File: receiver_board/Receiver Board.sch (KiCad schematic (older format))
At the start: 12 parts, among them P4 SERIAL, SW1 SW_DPST, U1 LM3671, U2 ESP-01, U3 NeoPixel, U4 SN74LVC1T45

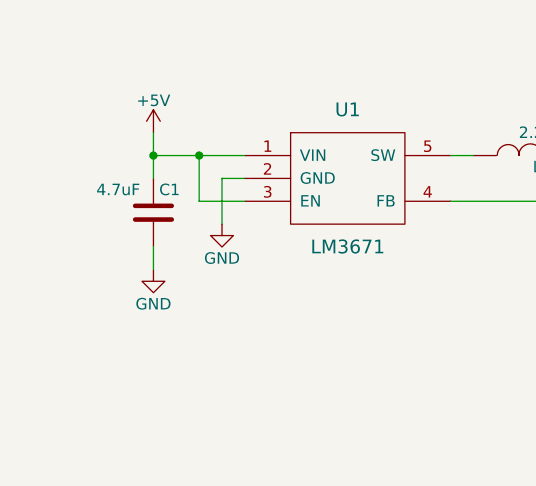
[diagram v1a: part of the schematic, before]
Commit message: Added BOM and fuse
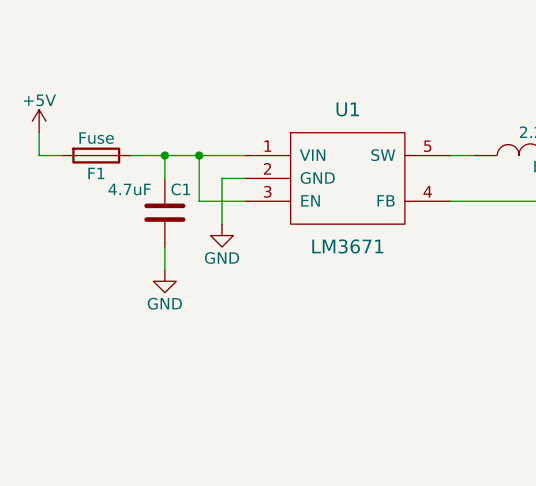
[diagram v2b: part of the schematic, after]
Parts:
- added F1: Fuse, Resistors_SMD:R_0805_HandSoldering, symbol Fuse
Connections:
- net +5V: now also F1.2; no longer C1.1, U1.1 (VIN), U1.3 (EN)
- new net: C1.1, F1.1, U1.1 (VIN), U1.3 (EN)
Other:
- moved on the sheet: C1
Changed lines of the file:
@@
 L C C1
 U 1 1 57A0E3BE
-P 3800 3250
-F 0 "C1" H 3825 3350 50  0000 L CNN
-F 1 "4.7uF" H 3550 3350 50  0000 L CNN
-F 2 "Capacitors_SMD:C_0805_HandSoldering" H 3800 4200 50  0001 C CNN
-F 3 "" H 3800 3250 50  0000 C CNN
-	1    3800 3250
+P 3850 3250
+F 0 "C1" H 3875 3350 50  0000 L CNN
+F 1 "4.7uF" H 3600 3350 50  0000 L CNN
+F 2 "Capacitors_SMD:C_0805_HandSoldering" H 3850 4200 50  0001 C CNN
+F 3 "" H 3850 3250 50  0000 C CNN
+	1    3850 3250
 	1    0    0    -1
 $EndComp
@@
 $EndComp
 $Comp
-L VCC #PWR6
+L VCC #PWR01
 U 1 1 5AF73AE7
 P 7350 2950
-F 0 "#PWR6" H 7350 2800 50  0001 C CNN
+F 0 "#PWR01" H 7350 2800 50  0001 C CNN
 F 1 "VCC" H 7350 3100 50  0000 C CNN
 F 2 "" H 7350 2950 50  0001 C CNN
@@
 $EndComp
 $Comp
-L GND #PWR8
+L GND #PWR02
 U 1 1 5AF73B1B
 P 8950 3950
-F 0 "#PWR8" H 8950 3700 50  0001 C CNN
+F 0 "#PWR02" H 8950 3700 50  0001 C CNN
 F 1 "GND" H 8950 3800 50  0000 C CNN
 F 2 "" H 8950 3950 50  0001 C CNN
@@
 Connection ~ 8950 3650
 Wire Wire Line
-	3800 3000 4200 3000
+	3700 3000 4200 3000
 Connection ~ 4000 3000
 Wire Wire Line
@@
 	4000 3000 4000 3200
 $Comp
-L +5V #PWR1
+L +5V #PWR03
 U 1 1 5AF7418F
-P 3800 2900
-F 0 "#PWR1" H 3800 2750 50  0001 C CNN
-F 1 "+5V" H 3800 3040 50  0000 C CNN
-F 2 "" H 3800 2900 50  0001 C CNN
-F 3 "" H 3800 2900 50  0001 C CNN
-	1    3800 2900
-	1    0    0    -1
-$EndComp
-Wire Wire Line
-	3800 2900 3800 3100
-Connection ~ 3800 3000
-$Comp
-L GND #PWR2
+P 3300 2900
+F 0 "#PWR03" H 3300 2750 50  0001 C CNN
+F 1 "+5V" H 3300 3040 50  0000 C CNN
+F 2 "" H 3300 2900 50  0001 C CNN
+F 3 "" H 3300 2900 50  0001 C CNN
+	1    3300 2900
+	1    0    0    -1
+$EndComp
+Wire Wire Line
+	3300 2900 3300 3000
+$Comp
+L GND #PWR04
 U 1 1 5AF743AA
-P 3800 3500
-F 0 "#PWR2" H 3800 3250 50  0001 C CNN
-F 1 "GND" H 3800 3350 50  0000 C CNN
-F 2 "" H 3800 3500 50  0001 C CNN
-F 3 "" H 3800 3500 50  0001 C CNN
-	1    3800 3500
-	1    0    0    -1
-$EndComp
-Wire Wire Line
-	3800 3400 3800 3500
-$Comp
-L GND #PWR3
+P 3850 3500
+F 0 "#PWR04" H 3850 3250 50  0001 C CNN
+F 1 "GND" H 3850 3350 50  0000 C CNN
+F 2 "" H 3850 3500 50  0001 C CNN
+F 3 "" H 3850 3500 50  0001 C CNN
+	1    3850 3500
+	1    0    0    -1
+$EndComp
+Wire Wire Line
+	3850 3400 3850 3500
+$Comp
+L GND #PWR05
 U 1 1 5AF7446C
 P 4100 3300
-F 0 "#PWR3" H 4100 3050 50  0001 C CNN
+F 0 "#PWR05" H 4100 3050 50  0001 C CNN
 F 1 "GND" H 4100 3150 50  0000 C CNN
 F 2 "" H 4100 3300 50  0001 C CNN
@@
 Connection ~ 5900 3200
 $Comp
-L GND #PWR5
+L GND #PWR06
 U 1 1 5AF746B4
 P 5900 3700
-F 0 "#PWR5" H 5900 3450 50  0001 C CNN
+F 0 "#PWR06" H 5900 3450 50  0001 C CNN
 F 1 "GND" H 5900 3550 50  0000 C CNN
 F 2 "" H 5900 3700 50  0001 C CNN
@@
 	5900 3600 5900 3700
 $Comp
-L VCC #PWR4
+L VCC #PWR07
 U 1 1 5AF74726
 P 5900 2900
-F 0 "#PWR4" H 5900 2750 50  0001 C CNN
+F 0 "#PWR07" H 5900 2750 50  0001 C CNN
 F 1 "VCC" H 5900 3050 50  0000 C CNN
 F 2 "" H 5900 2900 50  0001 C CNN
@@
 NoConn ~ 9400 3000
 $Comp
-L VCC #PWR7
+L VCC #PWR08
 U 1 1 5AF74CAE
 P 8750 2600
-F 0 "#PWR7" H 8750 2450 50  0001 C CNN
+F 0 "#PWR08" H 8750 2450 50  0001 C CNN
 F 1 "VCC" H 8750 2750 50  0000 C CNN
 F 2 "" H 8750 2600 50  0001 C CNN
@@
 Connection ~ 8750 3200
 $Comp
-L GND #PWR9
+L GND #PWR09
 U 1 1 5AF74D9B
 P 10000 3300
-F 0 "#PWR9" H 10000 3050 50  0001 C CNN
+F 0 "#PWR09" H 10000 3050 50  0001 C CNN
 F 1 "GND" H 10000 3150 50  0000 C CNN
 F 2 "" H 10000 3300 50  0001 C CNN
@@
 	7200 4500 7400 4500
 $Comp
-L +5V #PWR?
+L +5V #PWR010
 U 1 1 5AF754B5
 P 7200 4400
-F 0 "#PWR?" H 7200 4250 50  0001 C CNN
+F 0 "#PWR010" H 7200 4250 50  0001 C CNN
 F 1 "+5V" H 7200 4540 50  0000 C CNN
 F 2 "" H 7200 4400 50  0001 C CNN
@@
 	7300 4800 7100 4800
 $Comp
-L GND #PWR?
+L GND #PWR011
 U 1 1 5AF7558F
 P 7300 4900
-F 0 "#PWR?" H 7300 4650 50  0001 C CNN
+F 0 "#PWR011" H 7300 4650 50  0001 C CNN
 F 1 "GND" H 7300 4750 50  0000 C CNN
 F 2 "" H 7300 4900 50  0001 C CNN
@@
 Connection ~ 7300 4800
 $Comp
-L GND #PWR?
+L GND #PWR012
 U 1 1 5AF75675
 P 8600 4800
-F 0 "#PWR?" H 8600 4550 50  0001 C CNN
+F 0 "#PWR012" H 8600 4550 50  0001 C CNN
 F 1 "GND" H 8600 4650 50  0000 C CNN
 F 2 "" H 8600 4800 50  0001 C CNN
@@
 	8600 4600 8600 4800
 $Comp
-L VCC #PWR?
+L VCC #PWR013
 U 1 1 5AF7570E
 P 8600 4400
-F 0 "#PWR?" H 8600 4250 50  0001 C CNN
+F 0 "#PWR013" H 8600 4250 50  0001 C CNN
 F 1 "VCC" H 8600 4550 50  0000 C CNN
 F 2 "" H 8600 4400 50  0001 C CNN
@@
 Wire Wire Line
 	8600 4500 8500 4500
+$Comp
+L Fuse F1
+U 1 1 5AF9F066
+P 3550 3000
+F 0 "F1" V 3630 3000 50  0000 C CNN
+F 1 "Fuse" V 3475 3000 50  0000 C CNN
+F 2 "Resistors_SMD:R_0805_HandSoldering" V 3480 3000 50  0001 C CNN
+F 3 "" H 3550 3000 50  0001 C CNN
+	1    3550 3000
+	0    1    1    0
+$EndComp
+Wire Wire Line
+	3300 3000 3400 3000
+Wire Wire Line
+	3850 3100 3850 3000
+Connection ~ 3850 3000
 $EndSCHEMATC
